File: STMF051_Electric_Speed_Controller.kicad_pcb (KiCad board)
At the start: 4 copper layers, 46 x 47 mm, 164 parts, among them J1 Conn_01x03_Pin, J2 Conn_01x03_Pin, J3 Conn_01x03_Pin, J4 Conn_01x03_Pin, J5 Conn_01x03_Pin, J6 Conn_01x03_Pin, Q1 TPH3R704PL,L1Q, Q10 TPH3R704PL,L1Q, Q11 TPH3R704PL,L1Q, Q12 TPH3R704PL,L1Q, Q2 TPH3R704PL,L1Q, Q3 TPH3R704PL,L1Q, Q4 TPH3R704PL,L1Q, Q5 TPH3R704PL,L1Q, Q6 TPH3R704PL,L1Q, Q7 TPH3R704PL,L1Q, Q8 TPH3R704PL,L1Q, Q9 TPH3R704PL,L1Q, SW1 EVPAA602, SW2 EVPAA602, U1 MAX20008AFOA/VY+, U2 AP63205WU, U3 AP63203WU, U4 STM32F051K8Tx, U5 FD6288Q, U6 STM32F051K8Tx, U7 FD6288Q, U8 INA190A4IDCKR

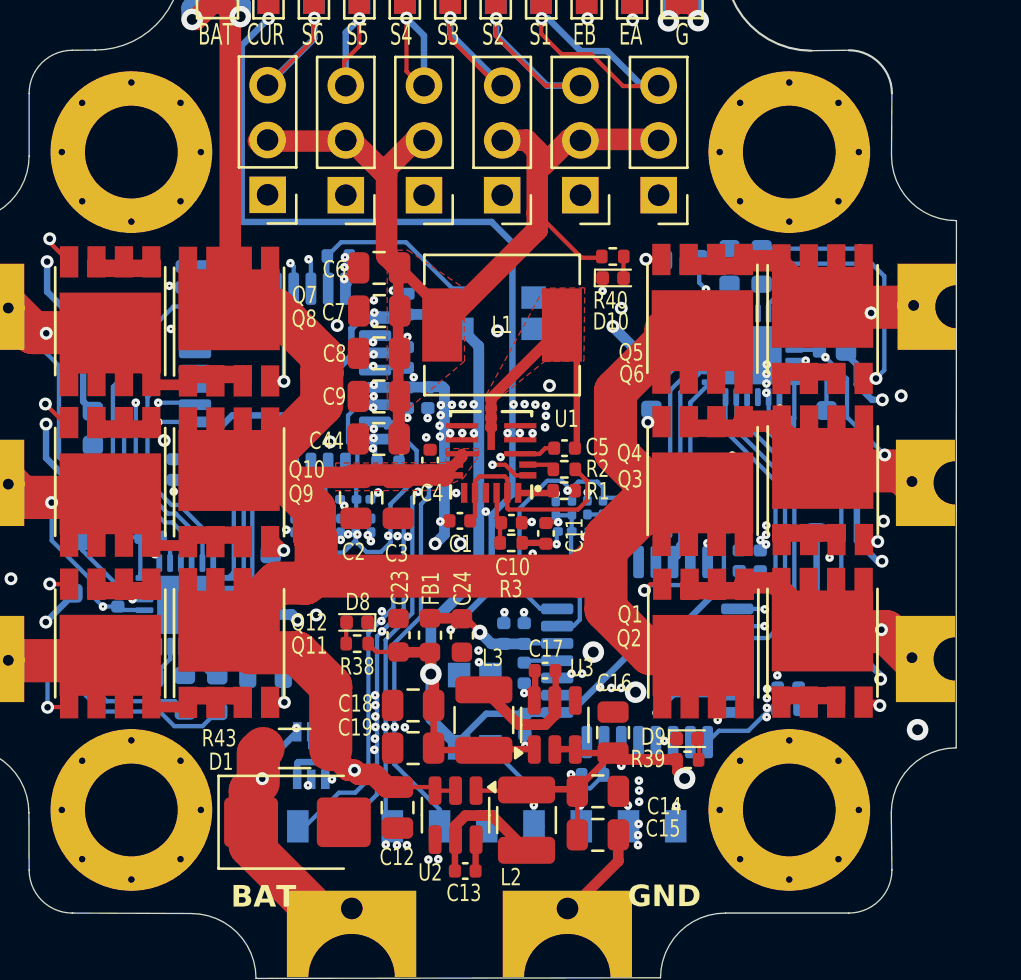
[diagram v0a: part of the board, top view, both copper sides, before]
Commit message: add logo and use 0603 LEDs
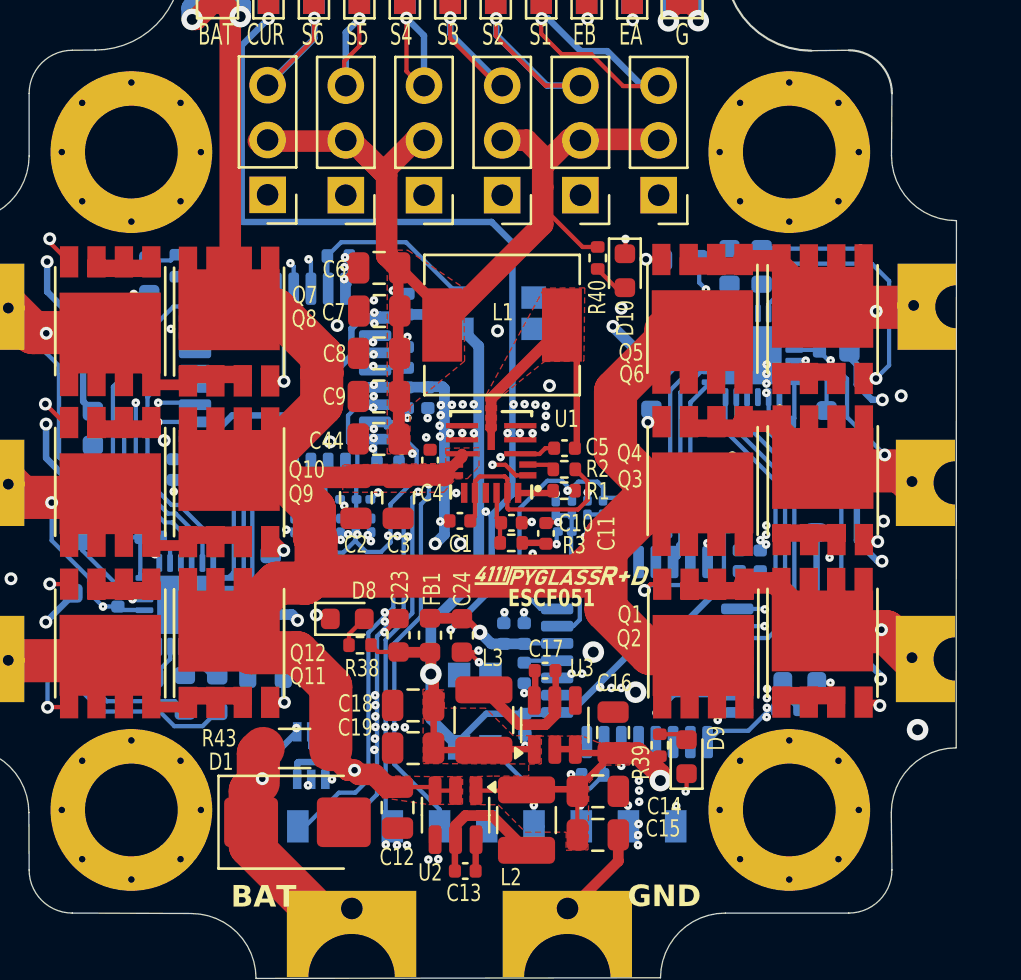
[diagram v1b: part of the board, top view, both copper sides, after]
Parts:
- added G***: LOGO, ProjectLibrary:spyglass10, F.Cu at (104.8, 106.3)
- added G***: LOGO, ProjectLibrary:spyglass15, B.Cu at (100.7, 91.0)
- D10, D11, D12, D8, D9: footprint ProjectLibrary:LED_0402_1005Metric -> LED_SMD:LED_0603_1608Metric
- moved D11 1.54 mm to (85.6, 91.6)
- moved R39 1.46 mm to (109.2, 113.2), turned to 90 degrees
- moved R41 1.33 mm to (86.8, 91.0)
- moved D9 0.83 mm to (110.5, 113.8), turned to 90 degrees
- moved R40 0.70 mm to (106.4, 90.7), turned to -90 degrees
- moved D10 0.64 mm to (107.6, 91.2), turned to -90 degrees
- moved D12 0.61 mm to (115.7, 110.3), turned to 180 degrees
- moved D8 0.48 mm to (94.8, 107.4), turned to 0 degrees
- moved D4 0.16 mm to (118.0, 94.2)
- moved R38 0.15 mm to (95.3, 108.6)
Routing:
- net GND: track 31.7 -> 38.2 mm
- net VDC: track 58.9 -> 57.4 mm
- net Net-(U6-PA15): track 0.96 -> 2.46 mm
- net Net-(D10-A): track 1.01 -> 1.63 mm
- net Net-(D12-A): track 1.09 -> 1.67 mm
- net Net-(D8-A): track 1.00 -> 1.51 mm
- added copper zone on F.Cu, net +3.3V
- added copper zone on F.Cu, net +5V
- added copper zone on F.Cu, net +VBAT
- removed copper zone on F.Cu, net +BATT
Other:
- board text added: "ESCF051"
- board text added: "ESCF051 mgi 07/24"

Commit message: change LED footprint to 0603 and change D1 to more powerful diode with same footprint
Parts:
- D1: value SMBJ28A -> 1.5SMBJ26A-H
- moved R38 0.07 mm to (95.3, 108.7)
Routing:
- net GND: track 38.2 -> 44.2 mm, vias 144 -> 147
- net +5V: track 186.1 -> 187.2 mm

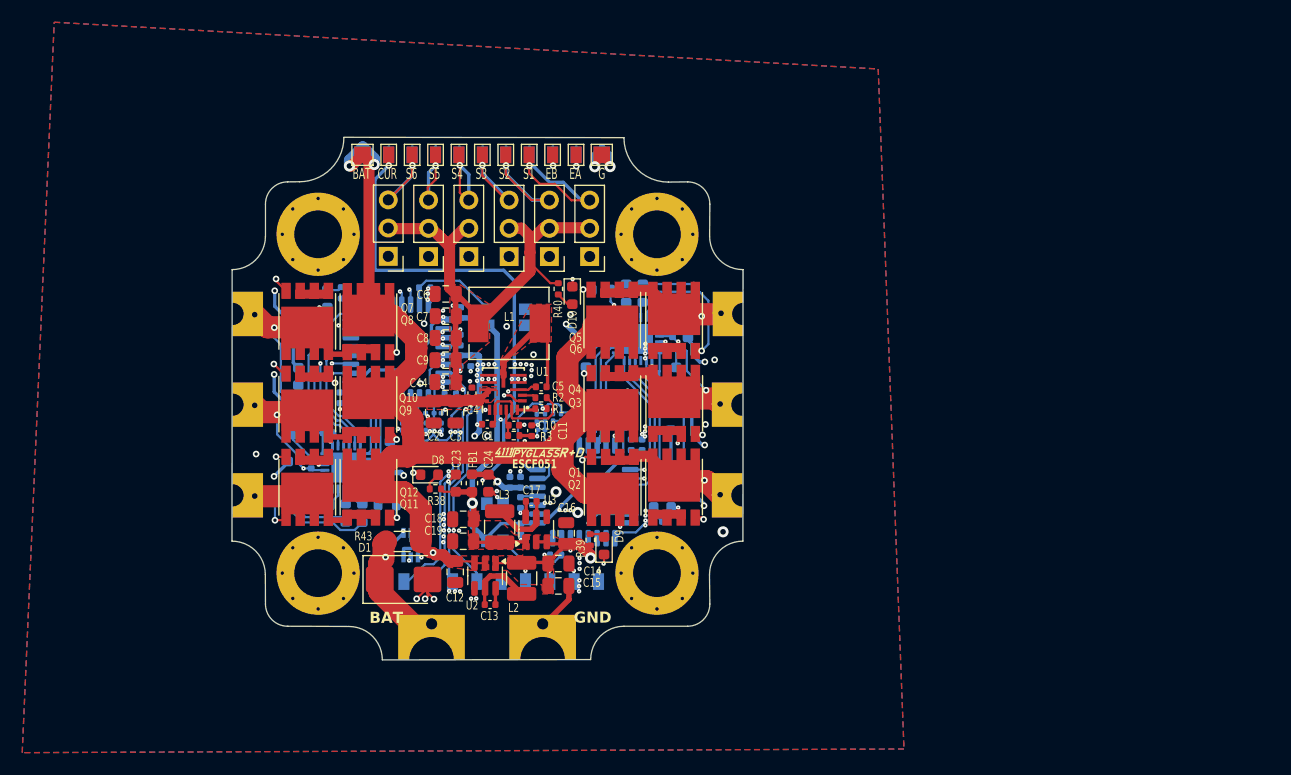
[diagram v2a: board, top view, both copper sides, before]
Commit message: edit layout A to work without blind vias by turing MC and ESC 45 to take advantage of pin layouts
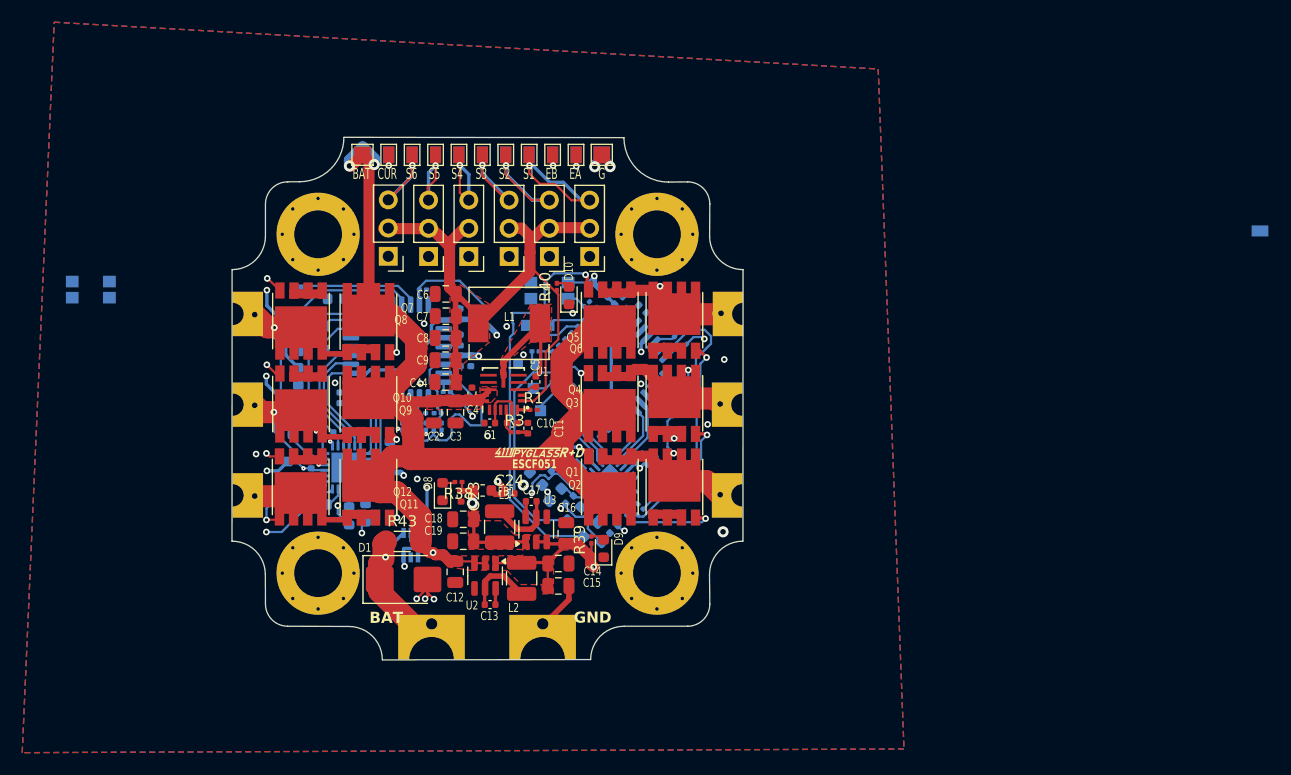
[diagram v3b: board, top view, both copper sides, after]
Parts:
- removed R2: 22k0, Resistor_SMD:R_0402_1005Metric
- C23, C24: footprint Capacitor_SMD:C_0603_1608Metric -> Capacitor_SMD:C_0402_1005Metric
- R1, R21, R22, R3, R38, R39, R4, R40, R41, R42, R5: footprint Resistor_SMD:R_0402_1005Metric -> ProjectLibrary:R_0201_0603Metric
- R15, R18, R20: footprint Resistor_SMD:R_0603_1608Metric -> ProjectLibrary:R_0201_0603Metric
- TP10, TP11, TP3, TP4, TP8, TP9: footprint ProjectLibrary:TestPoint_Pad_1.0x1.5mm -> TestPoint:TestPoint_Pad_1.0x1.0mm
- TP5: renamed from TP6; footprint ProjectLibrary:TestPoint_Pad_1.0x1.5mm -> TestPoint:TestPoint_Pad_1.0x1.0mm
- TP6: renamed from TP7; footprint ProjectLibrary:TestPoint_Pad_1.0x1.5mm -> TestPoint:TestPoint_Pad_1.0x1.0mm
- moved TP12 75.2 mm to (169.5, 85.5), turned to -90 degrees
- moved SW2 37.5 mm to (64.3, 90.7)
- moved TP9 30.8 mm to (83.0, 90.8), turned to -90 degrees
- moved TP8 27.9 mm to (83.0, 92.8), turned to -90 degrees
- moved TP10 24.8 mm to (85.3, 94.0), turned to -90 degrees
- moved TP4 23.2 mm to (105.5, 94.0), turned to 0 degrees
- moved TP3 23.2 mm to (103.5, 94.0), turned to 0 degrees
- moved R5 22.8 mm to (109.0, 92.0), turned to 45 degrees
- moved C21 22.4 mm to (111.8, 91.7), turned to 45 degrees
- moved TP11 22.0 mm to (85.3, 96.2), turned to -90 degrees
- moved R19 21.6 mm to (109.3, 112.3), turned to 45 degrees
- moved D4 21.5 mm to (109.7, 114.0), turned to -135 degrees
- moved SW1 21.4 mm to (105.6, 90.8), turned to 180 degrees
- moved C25 20.6 mm to (114.0, 92.5), turned to -45 degrees
- moved C27 20.4 mm to (115.9, 93.1), turned to -45 degrees
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- renumbered TP5 to TP7
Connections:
- net Net-(Q1-Pad4) renamed /FET Driver/HOGate01_A
- net Net-(Q10-Pad4) renamed /FET Driver/LOGate02_B
- net Net-(Q11-Pad4) renamed /FET Driver/HOGate03_B
- net Net-(Q12-Pad4) renamed /FET Driver/LOGate03_B
- net Net-(Q2-Pad4) renamed /FET Driver/LOGate01_A
- net Net-(Q3-Pad4) renamed /FET Driver/HOGate02_A
- net Net-(Q4-Pad4) renamed /FET Driver/LOGate02_A
- net Net-(Q5-Pad4) renamed /FET Driver/HOGate03_A
- net Net-(Q6-Pad4) renamed /FET Driver/LOGate03_A
- net Net-(Q7-Pad4) renamed /FET Driver/HOGate01_B
- net Net-(Q8-Pad4) renamed /FET Driver/LOGate01_B
- net Net-(Q9-Pad4) renamed /FET Driver/HOGate02_B
- SW1 pad 1: /MCU/BOOT0_A -> +3.3V
- SW1 pad 2: +3.3V -> /MCU/BOOT0_A
- U1 pad 2: Net-(U1-*RESET) -> unconnected-(U1-*RESET-Pad2)
- U4 pad 18: HIN1_A -> HIN3_A
- U4 pad 20: HIN3_A -> HIN1_A
- U6 pad 18: HIN1_B -> HIN3_B
- U6 pad 20: HIN3_B -> HIN1_B
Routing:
- net +5V: track 187.2 -> 141.4 mm, vias 9 -> 7
- net +3.3VA: track 22.1 -> 65.1 mm, vias 2 -> 3
- net /FET Driver/HOGate03_A: track 1.81 -> 36.3 mm
- net SWCLK_B: track 29.8 -> 2.65 mm, vias 2 -> 0
- net GND: track 44.2 -> 17.7 mm, vias 147 -> 21
- net SWDIO_B: track 29.5 -> 3.63 mm, vias 2 -> 0
- net PHASE1_A: track 34.6 -> 58.6 mm, vias 3 -> 2
- net /FET Driver/HOGate02_A: track 1.32 -> 23.0 mm
- net RX1_B: track 32.2 -> 11.2 mm, vias 2 -> 0
- net TX1_B: track 31.3 -> 11.0 mm, vias 2 -> 0
- net PHASE3_B: track 35.1 -> 16.1 mm
- net /FET Driver/LOGate01_B: track 23.7 -> 6.45 mm
- net /FET Driver/LOGate02_B: track 20.2 -> 3.66 mm
- net CURR: track 52.6 -> 36.8 mm, vias 3 -> 2
- net /FET Driver/LOGate01_A: track 22.3 -> 7.76 mm, vias 2 -> 1
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
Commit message: removed all microvias, use 0603 for driver resistors
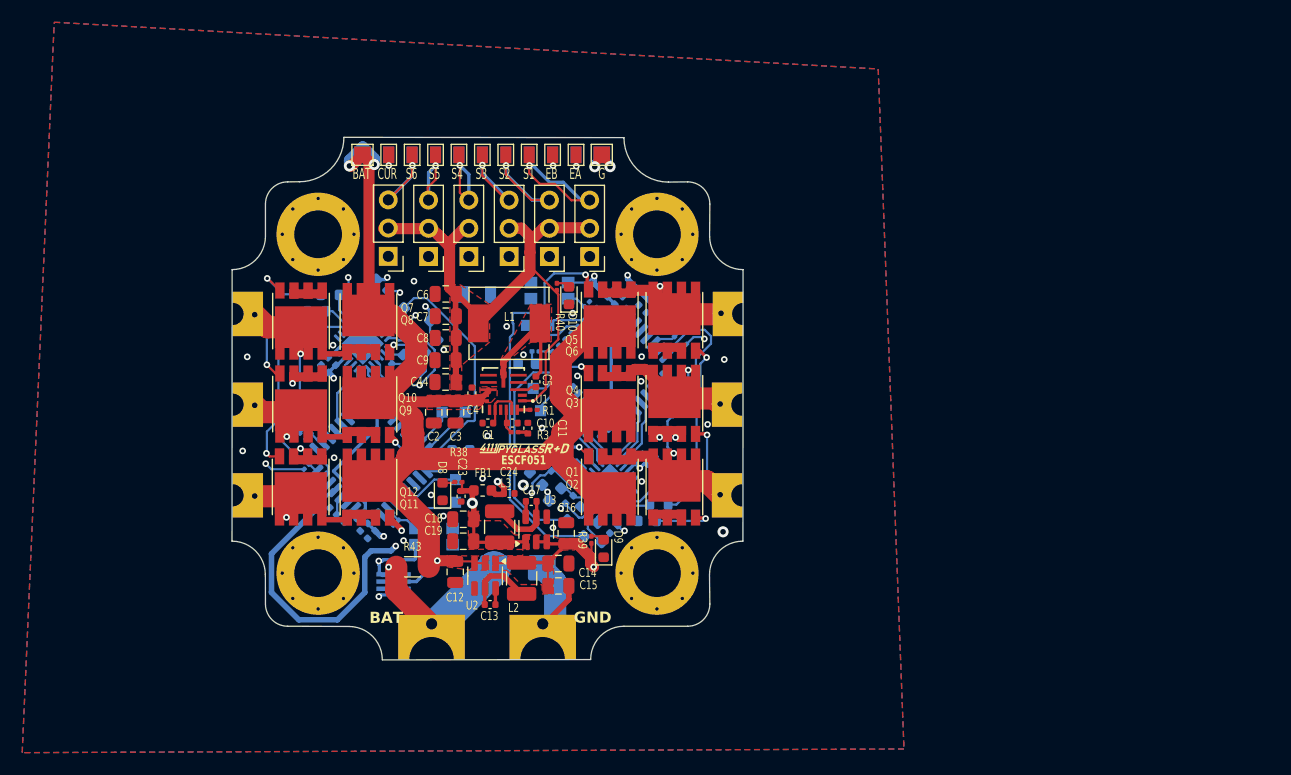
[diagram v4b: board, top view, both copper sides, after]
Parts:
- removed the G*** at (100.7, 91.0)
- D1: moved to B.Cu
- R15, R18, R20: footprint ProjectLibrary:R_0201_0603Metric -> Resistor_SMD:R_0603_1608Metric
- moved TP12 69.5 mm to (100.3, 91.2), turned to 180 degrees
- moved SW2 38.1 mm to (95.2, 113.0)
- moved TP7 26.9 mm to (97.8, 91.2)
- moved TP9 23.8 mm to (97.1, 109.9), turned to 0 degrees
- moved R21 21.1 mm to (91.8, 111.7), turned to -135 degrees
- moved TP8 20.6 mm to (97.1, 107.8), turned to 0 degrees
- moved C34 19.3 mm to (86.8, 111.3), turned to 135 degrees
- moved C38 19.3 mm to (84.8, 110.7), turned to -45 degrees
- moved R33 18.9 mm to (85.8, 91.2)
- moved R35 18.6 mm to (84.6, 92.7), turned to 0 degrees
- moved D7 18.2 mm to (89.4, 90.4), turned to 45 degrees
- moved R36 17.9 mm to (90.5, 91.4), turned to -135 degrees
- moved C37 17.7 mm to (85.5, 110.0), turned to -45 degrees
- moved D11 17.6 mm to (97.6, 105.2), turned to 180 degrees
- moved R37 17.6 mm to (83.5, 94.1), turned to 0 degrees
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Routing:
- net /FET Driver/HOGate03_B: track 2.76 -> 30.1 mm, vias 1 -> 2
- net PHASE3_B: track 16.1 -> 43.0 mm, vias 3 -> 2
- net /FET Driver/HOGate02_B: track 1.49 -> 25.4 mm
- net PWM2: track 31.9 -> 54.5 mm
- net PHASE2_B: track 18.2 -> 38.6 mm, vias 3 -> 2
- net +5V: track 141.4 -> 122.6 mm, vias 7 -> 6
- net PHASE1_B: track 23.1 -> 40.2 mm, vias 3 -> 2
- net CURR: track 36.8 -> 48.7 mm
- net +3.3VA: track 65.1 -> 77.0 mm
- net /FET Driver/LOGate03_B: track 2.41 -> 13.7 mm, vias 2 -> 1
- net /FET Driver/HOGate01_B: track 12.6 -> 4.34 mm
- net +3.3V: track 88.9 -> 96.3 mm
- net /MCU/BOOT0_B: track 9.07 -> 3.23 mm
- net +BATT: track 13.3 -> 19.1 mm
- net RX1_B: track 11.2 -> 5.90 mm
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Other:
- board text removed: "ESCF051 mgi 07/24"
- board text removed: "RX1A"
- board text removed: "RX1B"
- board text removed: "SCA"
- board text removed: "SCB"
- board text removed: "SDA"
- board text removed: "SDB"
- board text removed: "TX1A"
- board text removed: "TX1B"

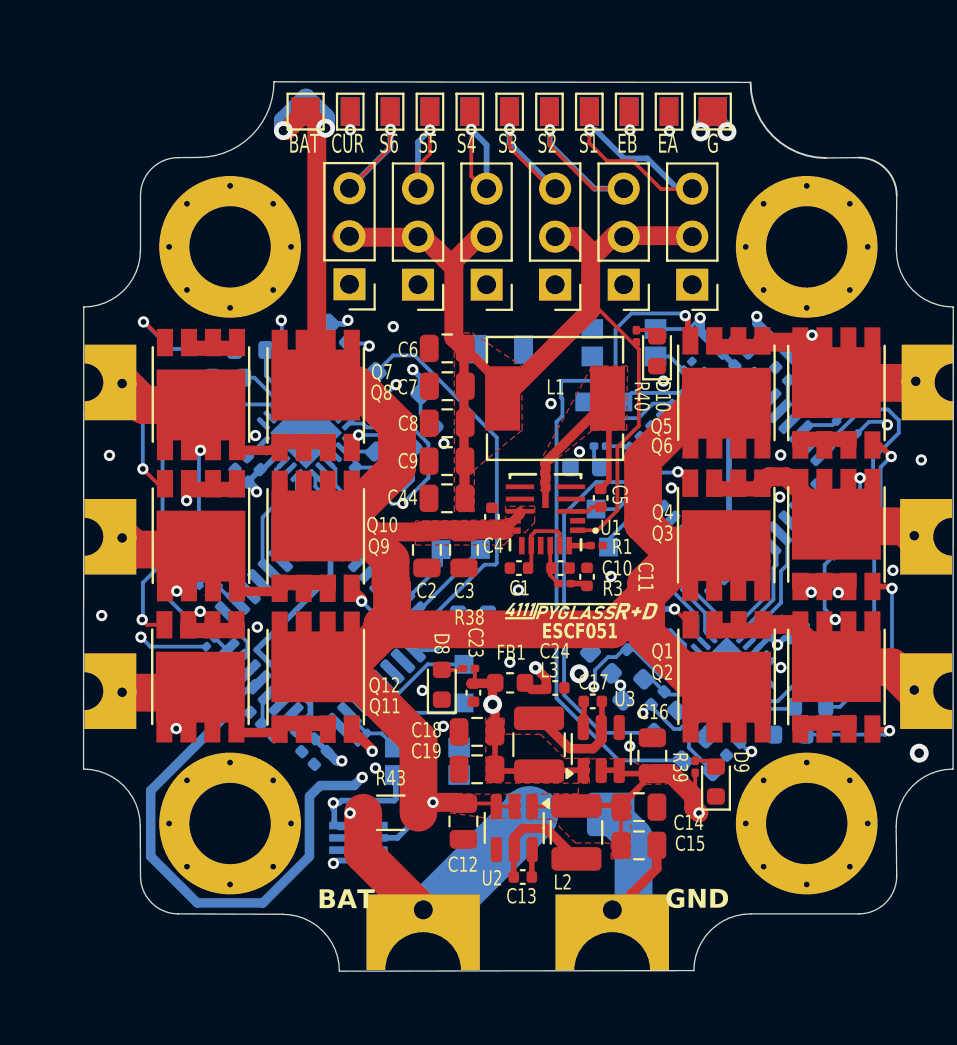
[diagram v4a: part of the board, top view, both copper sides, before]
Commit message: add gnd vias
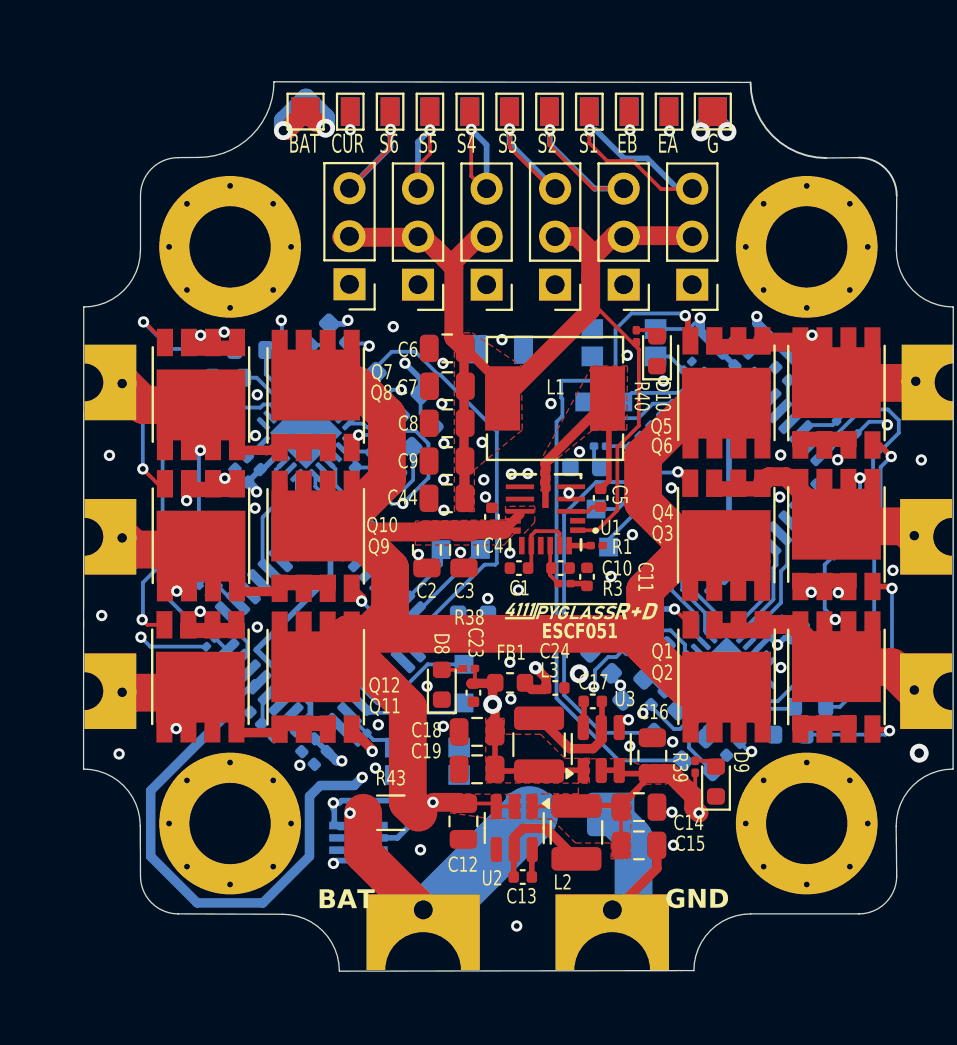
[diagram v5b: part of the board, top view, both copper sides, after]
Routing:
- net +VBAT: track 126.3 -> 116.5 mm
- net CURR: track 48.7 -> 55.3 mm
- net +3.3V: track 96.3 -> 98.3 mm
- net PHASE1_A: track 58.7 -> 60.5 mm
- net +5V: track 122.6 -> 123.3 mm
- net PHASE2_B: track 38.6 -> 38.0 mm
- net /FET Driver/HOGate02_B: track 25.4 -> 25.9 mm
- net GND: vias 30 -> 63
- added copper zone on In1.Cu, net +VBAT
- removed copper zone on In1.Cu, net GND

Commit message: tweaks
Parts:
- moved C24 0.16 mm to (102.0, 108.9)
- moved FB1 0.16 mm to (99.6, 108.7)
- moved C13 0.08 mm to (100.2, 119.0)
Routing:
- net +3.3V: track 98.3 -> 96.2 mm
- net PWM2: track 54.5 -> 55.6 mm
- net PHASE2_B: track 38.0 -> 38.7 mm
- net GND: vias 63 -> 71
